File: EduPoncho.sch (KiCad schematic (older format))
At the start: 1 part

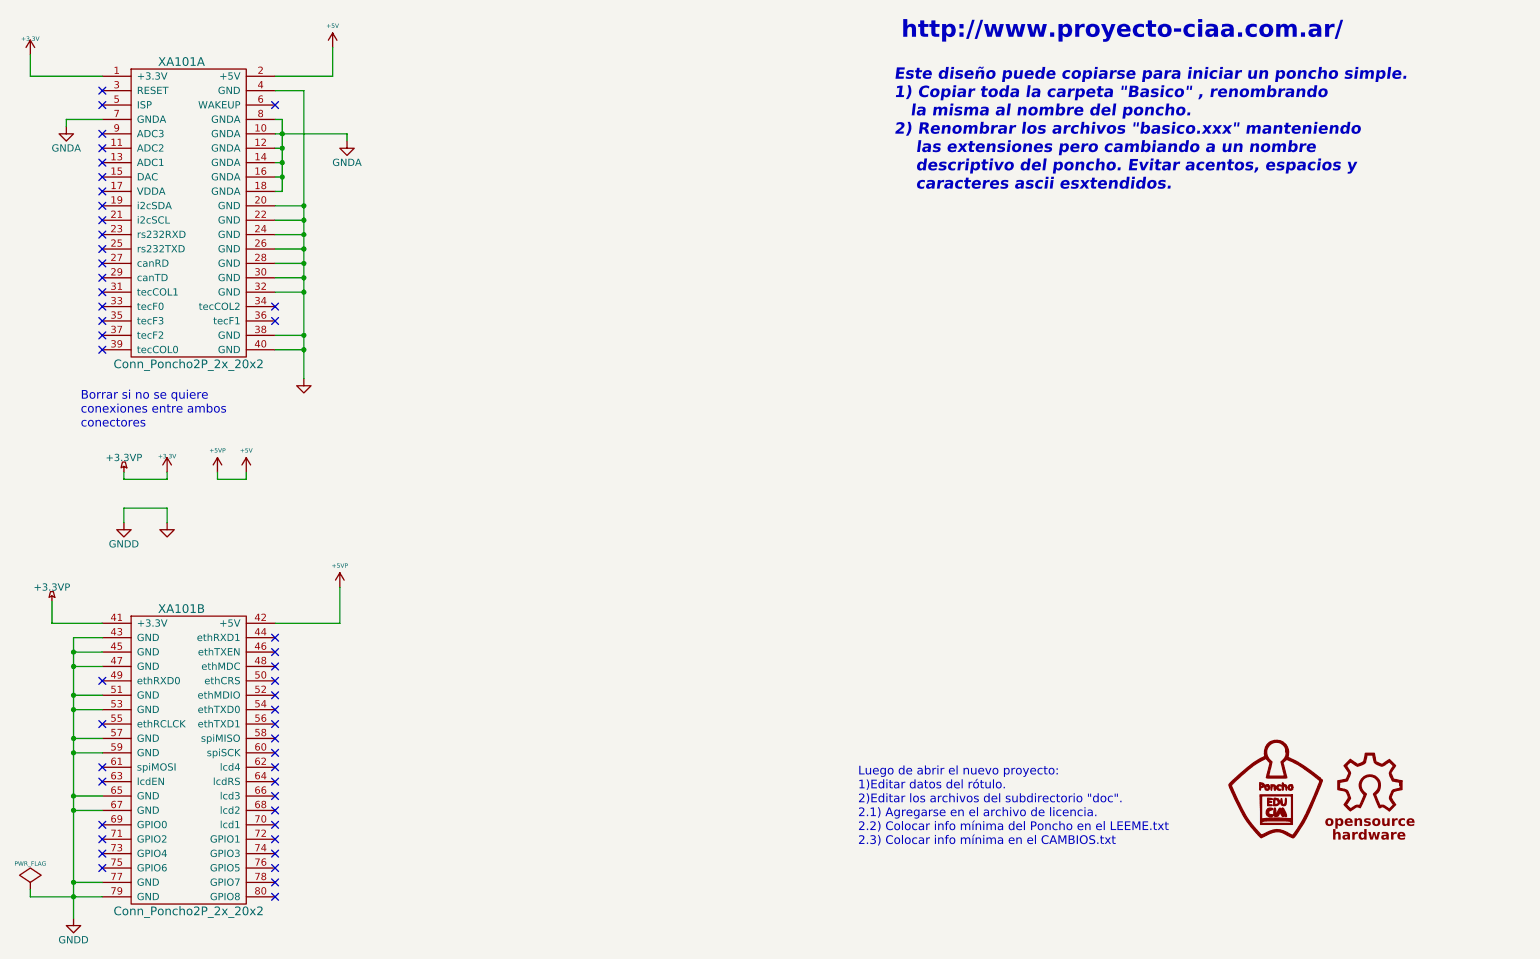
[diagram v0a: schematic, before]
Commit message: Se dividio el esquematico en bloques, se agrego conexion a reles y potenciometro
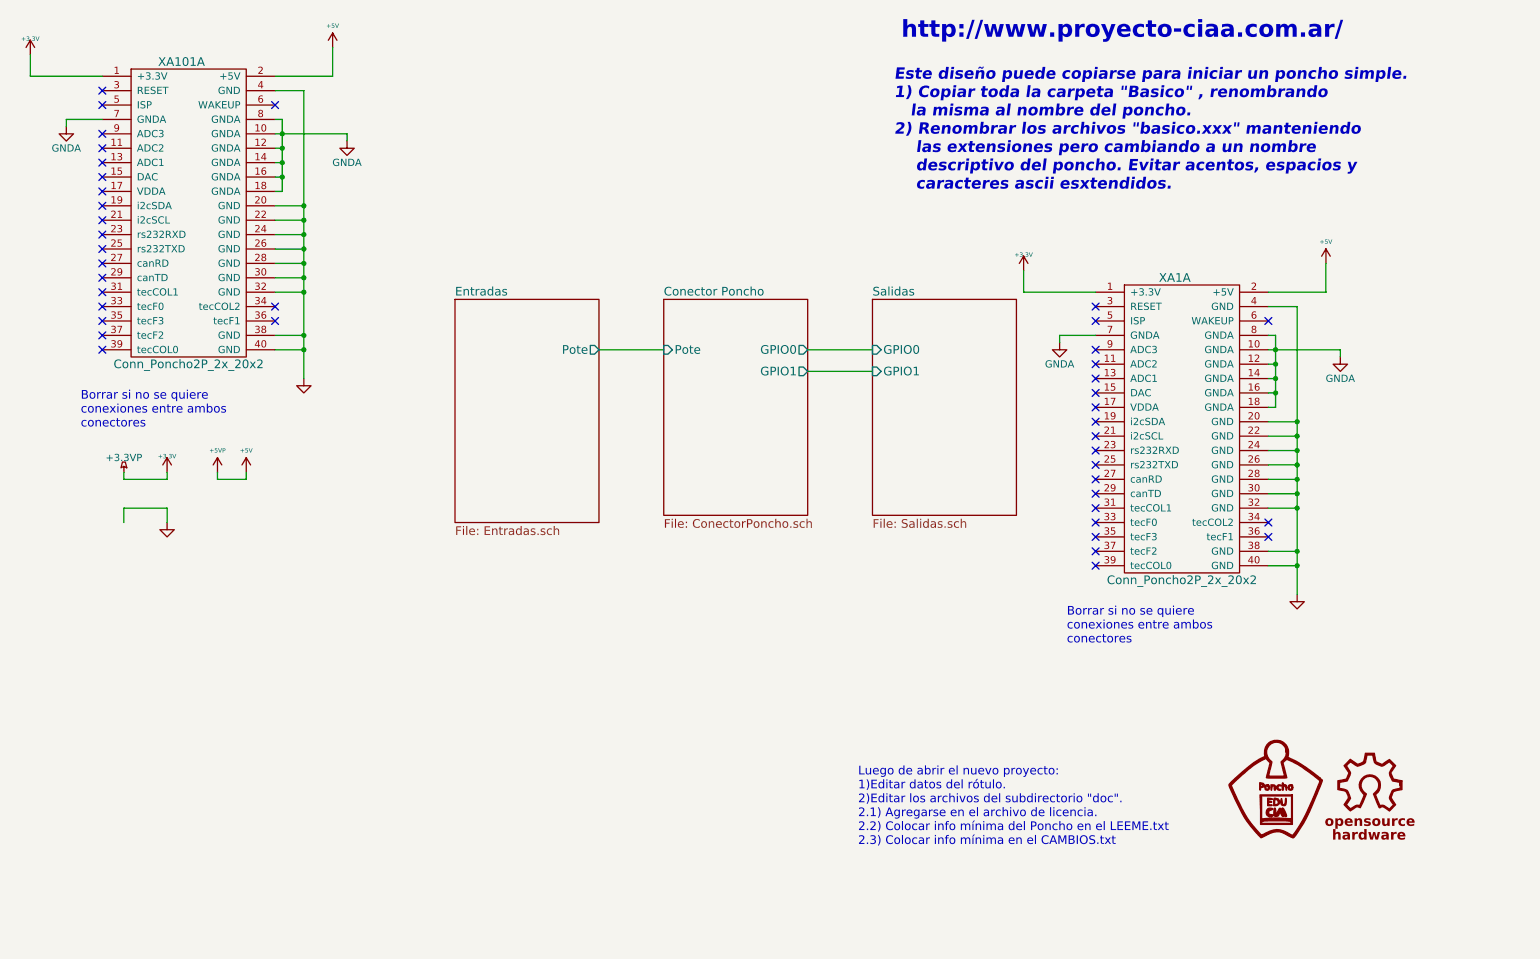
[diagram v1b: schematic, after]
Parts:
- removed unit 2 of XA101
- added XA1: Conn_Poncho2P_2x_20x2, footprint:Conn_Poncho_SinBorde, symbol Conn_Poncho2P_2x_20x2
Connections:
- net +3.3VP: now also XA1.1 (+3.3V)
- net +5V: now also XA1.2 (+5V)
- net GND: now also XA1.20 (GND), XA1.22 (GND), XA1.24 (GND), XA1.26 (GND), XA1.28 (GND), XA1.30 (GND), XA1.32 (GND), XA1.38 (GND), XA1.4 (GND), XA1.40 (GND)
- net GNDA: now also XA1.10 (GNDA), XA1.12 (GNDA), XA1.14 (GNDA), XA1.16 (GNDA), XA1.18 (GNDA), XA1.7 (GNDA), XA1.8 (GNDA)
- no-connect marks 48 -> 42

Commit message: Se completaron los circuitos esquematicos, falta revision.
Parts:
- removed XA1, XA101: Conn_Poncho2P_2x_20x2, footprint:Conn_Poncho_SinBorde, symbol Conn_Poncho2P_2x_20x2
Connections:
- net labels added: GNDD
- net labels removed: +3.3V, +3.3VP, +5VP, GNDA
- wire segments 62 -> 18
- no-connect marks 42 -> 0
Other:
- note removed: "Borrar si no se quiere \nconexiones entre ambos \nconectores"

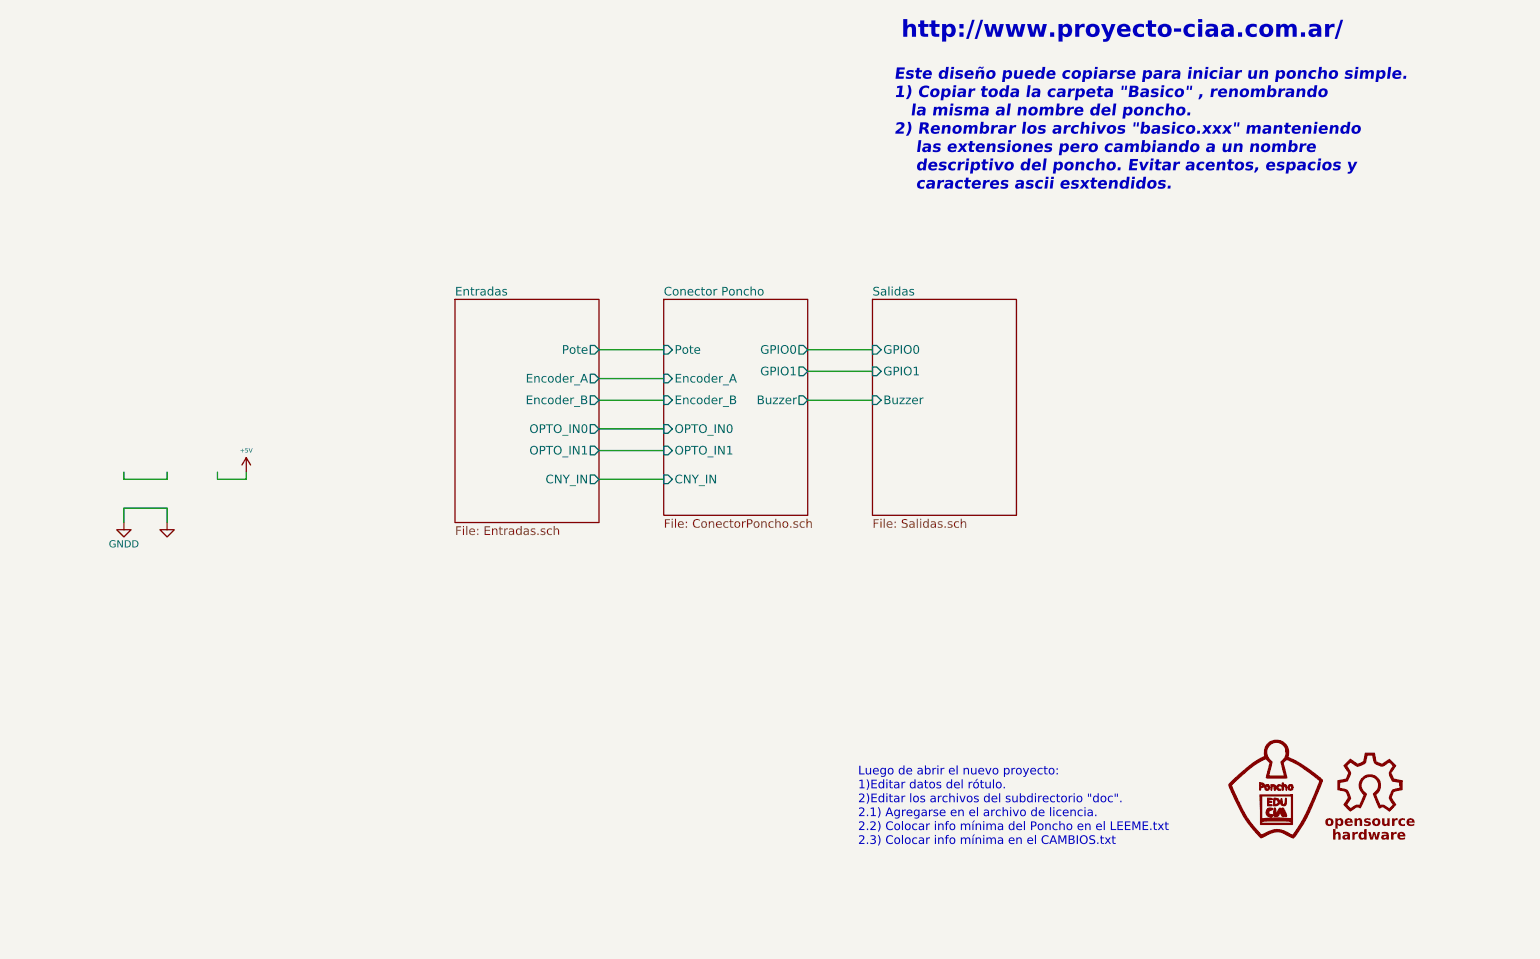
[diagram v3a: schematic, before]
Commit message: Correcion de errores, asignacion de footprints y ubicacion prelimilar de componentes.
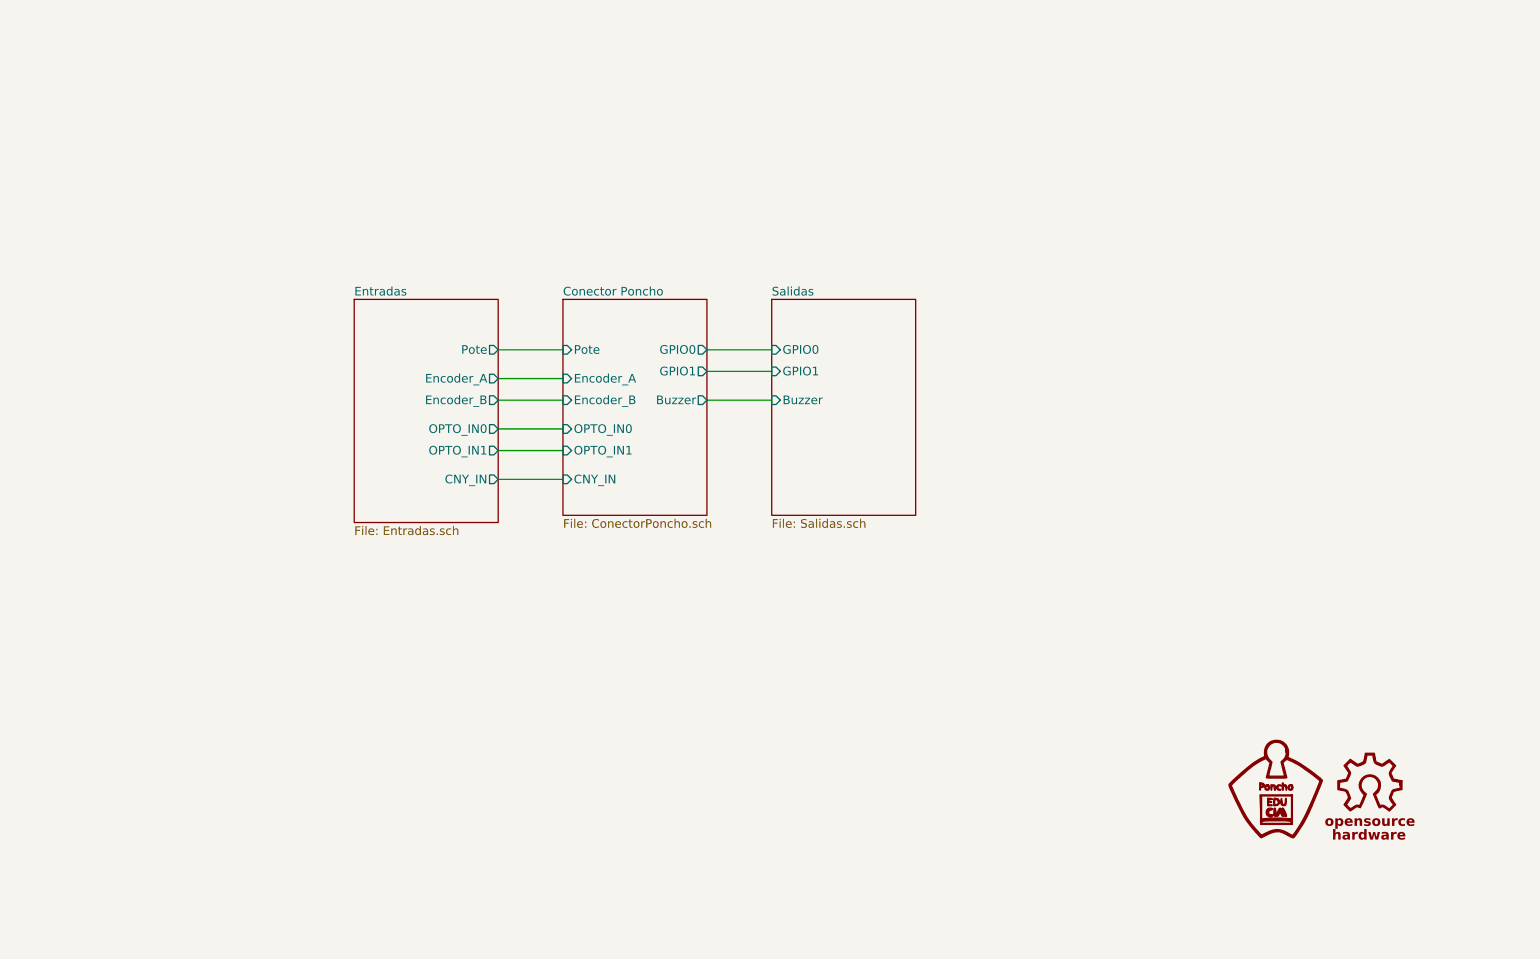
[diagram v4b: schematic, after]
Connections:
- net labels removed: +5V, GND, GNDD
- wire segments 18 -> 9
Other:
- note removed: "Este diseño puede copiarse para iniciar un poncho simple. \n1) Copiar toda la carpeta "Basico" , renombrando \n la misma al nombre del poncho.\n2) Renombrar los archivos "basico.xxx" manteniendo \n las extensiones pero cambiando a un nombre \n descriptivo del poncho. Evitar acentos, espacios y \n caracteres ascii esxtendidos."
- note removed: "Luego de abrir el nuevo proyecto:\n1)Editar datos del rótulo.\n2)Editar los archivos del subdirectorio "doc".\n2.1) Agregarse en el archivo de licencia.\n2.2) Colocar info mínima del Poncho en el LEEME.txt\n2.3) Colocar info mínima en el CAMBIOS.txt"
- note removed: "http://www.proyecto-ciaa.com.ar/"
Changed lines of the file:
@@
 EESchema Schematic File Version 2
-LIBS:device
 LIBS:power
-LIBS:sensors
-LIBS:ir
-LIBS:powerint
-LIBS:siliconi
-LIBS:switches
-LIBS:references
-LIBS:interface
-LIBS:cmos_ieee
-LIBS:analog_devices
-LIBS:nordicsemi
-LIBS:74xgxx
-LIBS:transistors
-LIBS:nxp_armmcu
-LIBS:logo
-LIBS:Power_Management
-LIBS:Altera
-LIBS:contrib
-LIBS:cmos4000
-LIBS:elec-unifil
-LIBS:graphic
-LIBS:display
-LIBS:dc-dc
-LIBS:opto
-LIBS:transf
-LIBS:analog_switches
-LIBS:regul
-LIBS:gennum
-LIBS:conn
-LIBS:relays
-LIBS:linear
-LIBS:ttl_ieee
-LIBS:valves
-LIBS:motor_drivers
-LIBS:adc-dac
-LIBS:texas
-LIBS:microchip_pic12mcu
-LIBS:actel
-LIBS:74xx
-LIBS:stm8
-LIBS:diode
-LIBS:ESD_Protection
-LIBS:microcontrollers
-LIBS:audio
-LIBS:microchip_dspic33dsc
-LIBS:pspice
-LIBS:xilinx
-LIBS:w_device
-LIBS:tvs
-LIBS:sw_push
-LIBS:s25fl032p0xmfi013
-LIBS:rs485_rs232_can
-LIBS:regulators
-LIBS:pbss5240xf
-LIBS:nsi50010yt1g
-LIBS:mcu-st
-LIBS:fqt13n06l
-LIBS:bat54_c
-LIBS:amesser-power
-LIBS:amesser-linear
-LIBS:amesser-discrete
-LIBS:amesser-conn
-LIBS:amesser-cmos4000
-LIBS:amesser-ad
-LIBS:Transil_diode
-LIBS:PS2805
-LIBS:BLM15HG6015N1D
-LIBS:93CXX
-LIBS:74LVC1G04GW
-LIBS:buzzer
-LIBS:ps2805-1
-LIBS:encoder_rotativo
 LIBS:EduPoncho-cache
 EELAYER 25 0
@@
 encoding utf-8
 Sheet 1 4
-Title "Poncho Básico (Editar y colocar el nombre final)"
-Date "2016-08-07"
+Title "EduPoncho"
+Date "2016-11-17"
 Rev "1.0"
 Comp "Proyecto CIAA - COMPUTADORA INDUSTRIAL ABIERTA ARGENTINA"
-Comment1 "https://github.com/ciaa/Ponchos/tree/master/Basico/doc"
+Comment1 "https://github.com/guille411/EduPoncho"
 Comment2 "Autores y Licencia del modelo (Diego Brengi - UNLaM)"
-Comment3 "Autor del poncho (COMPLETAR NOMBRE Y APELLIDO). Ver directorio \"doc\""
+Comment3 "Autor del poncho (Evangelista Guillermo). Ver directorio \"doc\""
 Comment4 ""
 $EndDescr
@@
 	1    0    0    -1
 $EndComp
-Text Notes 7500 1850 0    79   Italic 16
-Este diseño puede copiarse para iniciar un poncho simple. \n1) Copiar toda la carpeta "Basico" , renombrando \n   la misma al nombre del poncho.\n2) Renombrar los archivos "basico.xxx" manteniendo \n    las extensiones pero cambiando a un nombre \n    descriptivo del poncho. Evitar acentos, espacios y \n    caracteres ascii esxtendidos.
-Text Notes 7550 800  0    118  ~ 24
-http://www.proyecto-ciaa.com.ar/
-Text Notes 7250 6400 0    60   ~ 0
-Luego de abrir el nuevo proyecto:\n1)Editar datos del rótulo.\n2)Editar los archivos del subdirectorio "doc".\n2.1) Agregarse en el archivo de licencia.\n2.2) Colocar info mínima del Poncho en el LEEME.txt\n2.3) Colocar info mínima en el CAMBIOS.txt
-$Comp
-L +5V #PWR01
-U 1 1 57A7AAA1
-P 3000 3800
-F 0 "#PWR01" H 3000 3890 20  0001 C CNN
-F 1 "+5V" H 3000 3950 30  0000 C CNN
-F 2 "" H 3000 3800 60  0000 C CNN
-F 3 "" H 3000 3800 60  0000 C CNN
-	1    3000 3800
-	1    0    0    -1
-$EndComp
-Wire Wire Line
-	2150 3800 2150 3850
-Wire Wire Line
-	2150 3850 2450 3850
-Wire Wire Line
-	2450 3850 2450 3800
-Wire Wire Line
-	2800 3800 2800 3850
-Wire Wire Line
-	2800 3850 3000 3850
-Wire Wire Line
-	3000 3850 3000 3800
-$Comp
-L GND #PWR02
-U 1 1 57A7ADB5
-P 2450 4150
-F 0 "#PWR02" H 2450 4150 30  0001 C CNN
-F 1 "GND" H 2450 4080 30  0001 C CNN
-F 2 "" H 2450 4150 60  0000 C CNN
-F 3 "" H 2450 4150 60  0000 C CNN
-	1    2450 4150
-	1    0    0    -1
-$EndComp
-Wire Wire Line
-	2150 4150 2150 4050
-Wire Wire Line
-	2450 4050 2450 4150
-Wire Wire Line
-	2150 4050 2450 4050
 $Sheet
-S 4450 2600 1000 1550
+S 3750 2600 1000 1550
 U 581E4A63
 F0 "Entradas" 60
 F1 "Entradas.sch" 60
-F2 "Pote" O R 5450 2950 60
-F3 "Encoder_A" O R 5450 3150 60
-F4 "Encoder_B" O R 5450 3300 60
-F5 "OPTO_IN0" O R 5450 3500 60
-F6 "OPTO_IN1" O R 5450 3650 60
-F7 "CNY_IN" O R 5450 3850 60
+F2 "Pote" O R 4750 2950 60
+F3 "Encoder_A" O R 4750 3150 60
+F4 "Encoder_B" O R 4750 3300 60
+F5 "OPTO_IN0" O R 4750 3500 60
+F6 "OPTO_IN1" O R 4750 3650 60
+F7 "CNY_IN" O R 4750 3850 60
 $EndSheet
 $Sheet
-S 7350 2600 1000 1500
+S 6650 2600 1000 1500
 U 581E4ABE
 F0 "Salidas" 60
 F1 "Salidas.sch" 60
-F2 "GPIO0" I L 7350 2950 60
-F3 "GPIO1" I L 7350 3100 60
-F4 "Buzzer" I L 7350 3300 60
+F2 "GPIO0" I L 6650 2950 60
+F3 "GPIO1" I L 6650 3100 60
+F4 "Buzzer" I L 6650 3300 60
 $EndSheet
 $Sheet
-S 5900 2600 1000 1500
+S 5200 2600 1000 1500
 U 58255BD2
 F0 "Conector Poncho" 60
 F1 "ConectorPoncho.sch" 60
-F2 "GPIO0" O R 6900 2950 60
-F3 "GPIO1" O R 6900 3100 60
-F4 "Pote" I L 5900 2950 60
-F5 "Buzzer" O R 6900 3300 60
-F6 "Encoder_A" I L 5900 3150 60
-F7 "Encoder_B" I L 5900 3300 60
-F8 "OPTO_IN0" I L 5900 3500 60
-F9 "OPTO_IN1" I L 5900 3650 60
-F10 "CNY_IN" I L 5900 3850 60
+F2 "GPIO0" O R 6200 2950 60
+F3 "GPIO1" O R 6200 3100 60
+F4 "Pote" I L 5200 2950 60
+F5 "Buzzer" O R 6200 3300 60
+F6 "Encoder_A" I L 5200 3150 60
+F7 "Encoder_B" I L 5200 3300 60
+F8 "OPTO_IN0" I L 5200 3500 60
+F9 "OPTO_IN1" I L 5200 3650 60
+F10 "CNY_IN" I L 5200 3850 60
 $EndSheet
 Wire Wire Line
-	7350 2950 6900 2950
+	6650 2950 6200 2950
 Wire Wire Line
-	6900 3100 7350 3100
+	6200 3100 6650 3100
 Wire Wire Line
-	5900 2950 5450 2950
-$Comp
-L GNDD #PWR03
-U 1 1 58272F09
-P 2150 4150
-F 0 "#PWR03" H 2150 3900 50  0001 C CNN
-F 1 "GNDD" H 2150 4000 50  0000 C CNN
-F 2 "" H 2150 4150 50  0000 C CNN
-F 3 "" H 2150 4150 50  0000 C CNN
-	1    2150 4150
-	1    0    0    -1
-$EndComp
+	5200 2950 4750 2950
 Wire Wire Line
-	6900 3300 7350 3300
+	6200 3300 6650 3300
 Wire Wire Line
-	5450 3150 5900 3150
+	4750 3150 5200 3150
 Wire Wire Line
-	5450 3300 5900 3300
+	4750 3300 5200 3300
 Wire Wire Line
-	5450 3500 5900 3500
+	4750 3500 5200 3500
 Wire Wire Line
-	5900 3650 5450 3650
+	5200 3650 4750 3650
 Wire Wire Line
-	5900 3850 5450 3850
+	5200 3850 4750 3850
 $EndSCHEMATC

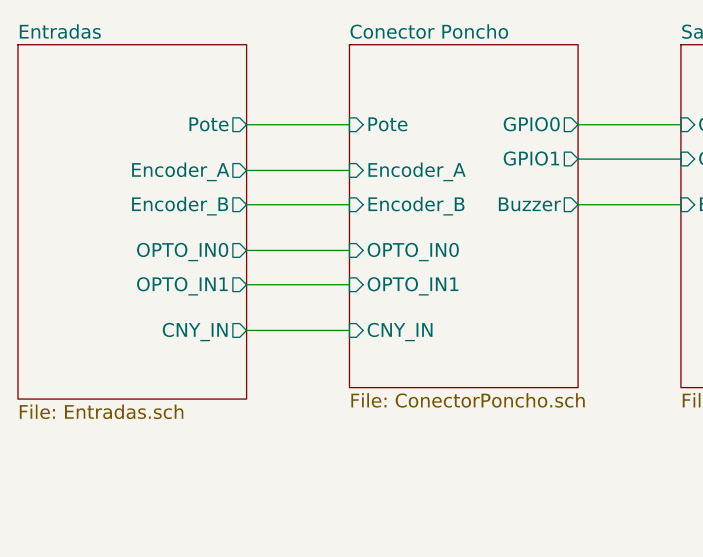
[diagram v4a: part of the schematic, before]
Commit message: Reubicacion de optoacopladores, cambio de footoprins de resistencias a 0805, correcion general.Falta arreglar archivos vista 3d y completar los campos #digikey
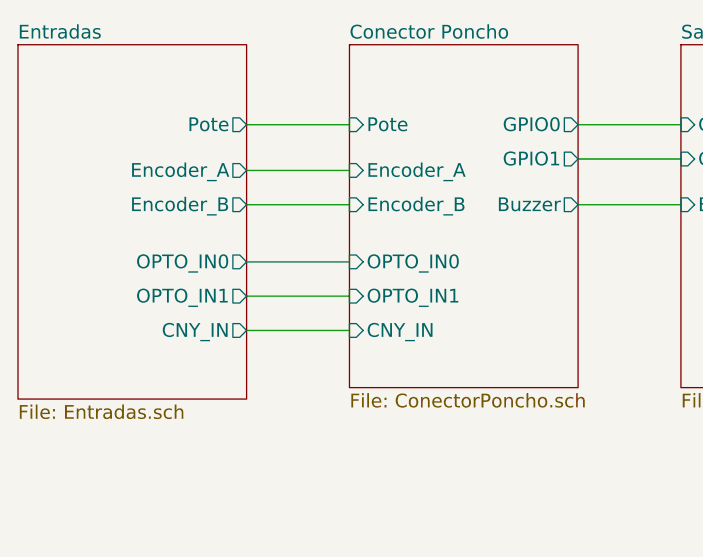
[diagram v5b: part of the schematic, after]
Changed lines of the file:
@@
 EESchema Schematic File Version 2
-LIBS:power
 LIBS:EduPoncho-cache
 EELAYER 25 0
@@
 Comment2 "Autores y Licencia del modelo (Diego Brengi - UNLaM)"
 Comment3 "Autor del poncho (Evangelista Guillermo). Ver directorio \"doc\""
-Comment4 ""
+Comment4 "Revisor: Martinez Horacio"
 $EndDescr
 $Comp
@@
 F3 "Encoder_A" O R 4750 3150 60
 F4 "Encoder_B" O R 4750 3300 60
-F5 "OPTO_IN0" O R 4750 3500 60
-F6 "OPTO_IN1" O R 4750 3650 60
-F7 "CNY_IN" O R 4750 3850 60
+F5 "OPTO_IN0" O R 4750 3550 60
+F6 "CNY_IN" O R 4750 3850 60
+F7 "OPTO_IN1" O R 4750 3700 60
 $EndSheet
 $Sheet
@@
 F6 "Encoder_A" I L 5200 3150 60
 F7 "Encoder_B" I L 5200 3300 60
-F8 "OPTO_IN0" I L 5200 3500 60
-F9 "OPTO_IN1" I L 5200 3650 60
-F10 "CNY_IN" I L 5200 3850 60
+F8 "OPTO_IN0" I L 5200 3550 60
+F9 "CNY_IN" I L 5200 3850 60
+F10 "OPTO_IN1" I L 5200 3700 60
 $EndSheet
 Wire Wire Line
@@
 	4750 3300 5200 3300
 Wire Wire Line
-	4750 3500 5200 3500
+	5200 3850 4750 3850
 Wire Wire Line
-	5200 3650 4750 3650
+	5200 3550 4750 3550
 Wire Wire Line
-	5200 3850 4750 3850
+	5200 3700 4750 3700
 $EndSCHEMATC
